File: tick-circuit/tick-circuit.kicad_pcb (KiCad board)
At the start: 2 copper layers, 45.7 x 33 mm, 14 parts, among them J1 Power, J2 50/60Hz, U1 74HCT4060, U2 74HCT73, X1 3.93216 MHz

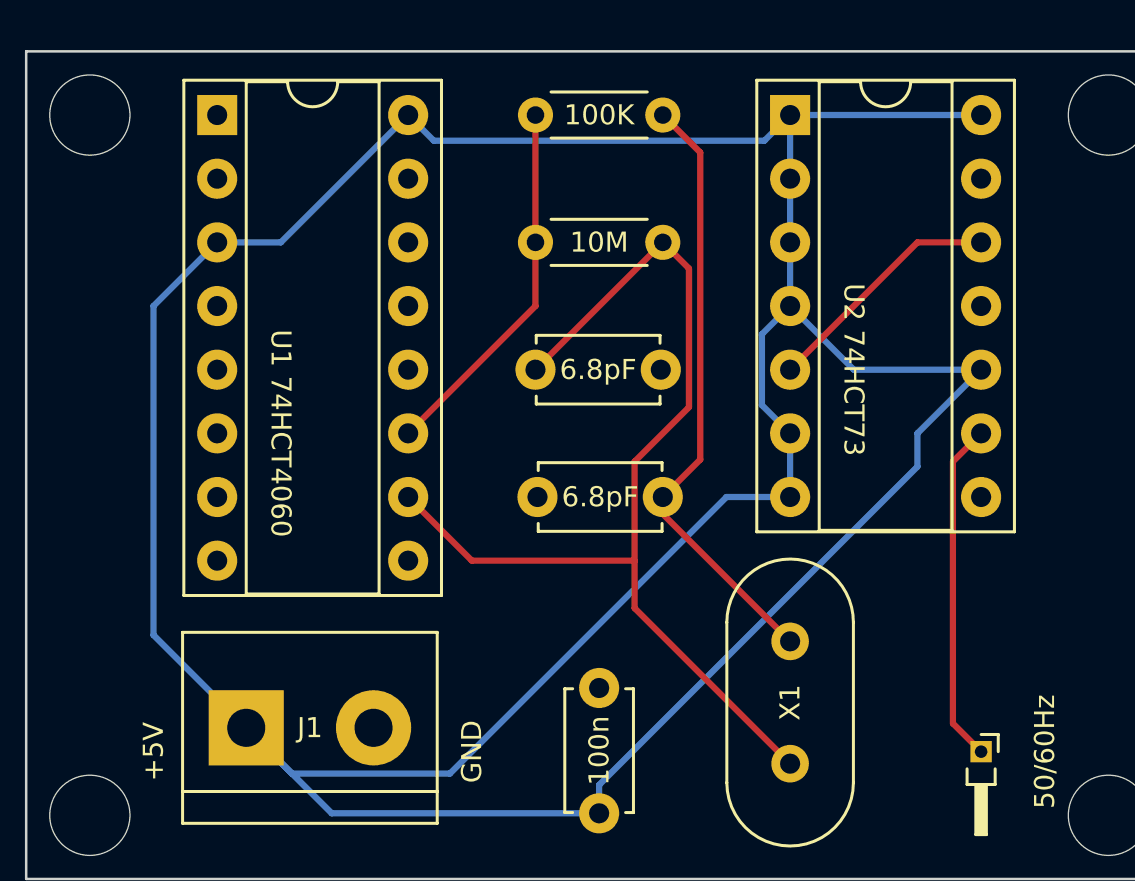
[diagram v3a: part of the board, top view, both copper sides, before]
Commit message: Misconnected +5v to the connection from U1 to U2, which would have sucked
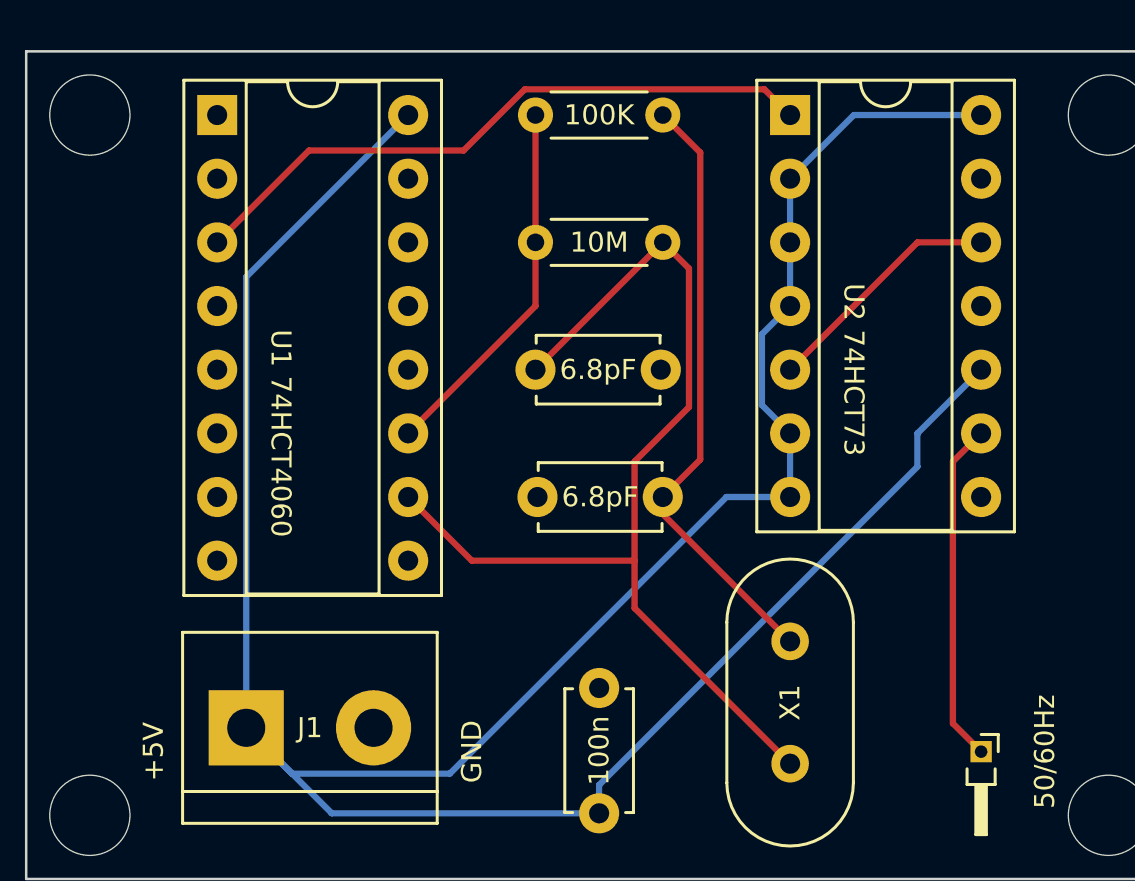
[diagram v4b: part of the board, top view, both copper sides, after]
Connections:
- U1 pad 3: +5V -> Net-(U1-Q13)
- U2 pad 1: +5V -> Net-(U1-Q13)
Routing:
- net +5V: track 146.8 -> 116.0 mm
- net Net-(U1-Q13): track 0.00 -> 25.8 mm
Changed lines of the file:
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@@
   (net 18 "unconnected-(U2A-~{Q}-Pad8)")
   (net 19 "unconnected-(U2B-~{Q}-Pad13)")
+  (net 20 "Net-(U1-Q13)")
   (footprint "Package_DIP:DIP-16_W7.62mm_Socket" (layer "F.Cu")
     (at 33.02 33.02)
@@
       (net 8 "unconnected-(U1-Q12-Pad2)") (pinfunction "Q12") (pintype "output+no_connect"))
     (pad "3" thru_hole oval (at 0 5.08) (size 1.6 1.6) (drill 0.8) (layers "*.Cu" "*.Mask")
-      (net 4 "+5V") (pinfunction "Q13") (pintype "output"))
+      (net 20 "Net-(U1-Q13)") (pinfunction "Q13") (pintype "output"))
     (pad "4" thru_hole oval (at 0 7.62) (size 1.6 1.6) (drill 0.8) (layers "*.Cu" "*.Mask")
       (net 9 "unconnected-(U1-Q5-Pad4)") (pinfunction "Q5") (pintype "output+no_connect"))
@@
       (net 6 "Net-(U1-RS)") (pinfunction "RS") (pintype "input"))
     (pad "12" thru_hole oval (at 7.62 10.16) (size 1.6 1.6) (drill 0.8) (layers "*.Cu" "*.Mask")
-      (net 2 "GND") (pinfunction "MR") (pintype "input"))
+      (net 2 "GND") (pinfunction "MR") (pintype "input") (thermal_bridge_angle 45))
     (pad "13" thru_hole oval (at 7.62 7.62) (size 1.6 1.6) (drill 0.8) (layers "*.Cu" "*.Mask")
       (net 14 "unconnected-(U1-Q8-Pad13)") (pinfunction "Q8") (pintype "output+no_connect"))
@@
       (stroke (width 0.1) (type solid)) (layer "F.Fab"))
     (pad "1" thru_hole rect (at 0 0) (size 1.6 1.6) (drill 0.8) (layers "*.Cu" "*.Mask")
-      (net 4 "+5V") (pinfunction "C") (pintype "input"))
+      (net 20 "Net-(U1-Q13)") (pinfunction "C") (pintype "input"))
     (pad "2" thru_hole oval (at 0 2.54) (size 1.6 1.6) (drill 0.8) (layers "*.Cu" "*.Mask")
       (net 4 "+5V") (pinfunction "~{R}") (pintype "input"))
@@
   (segment (start 60.96 47.04863) (end 60.96 45.72) (width 0.25) (layer "B.Cu") (net 4))
   (segment (start 37.59 60.88) (end 34.18 57.47) (width 0.25) (layer "B.Cu") (net 4))
-  (segment (start 58.42 43.18) (end 55.88 40.64) (width 0.25) (layer "B.Cu") (net 4))
-  (segment (start 63.5 43.18) (end 58.42 43.18) (width 0.25) (layer "B.Cu") (net 4))
-  (segment (start 54.855 34.045) (end 41.665 34.045) (width 0.25) (layer "B.Cu") (net 4))
-  (segment (start 33.02 38.1) (end 30.48 40.64) (width 0.25) (layer "B.Cu") (net 4))
-  (segment (start 30.48 40.64) (end 30.48 53.77) (width 0.25) (layer "B.Cu") (net 4))
+  (segment (start 58.42 33.02) (end 55.88 35.56) (width 0.25) (layer "B.Cu") (net 4))
+  (segment (start 40.64 33.02) (end 34.18 39.48) (width 0.25) (layer "B.Cu") (net 4))
   (segment (start 54.755 41.765) (end 55.88 40.64) (width 0.25) (layer "B.Cu") (net 4))
   (segment (start 48.26 60.88) (end 37.59 60.88) (width 0.25) (layer "B.Cu") (net 4))
-  (segment (start 55.88 33.02) (end 63.5 33.02) (width 0.25) (layer "B.Cu") (net 4))
   (segment (start 48.26 60.88) (end 48.26 59.74863) (width 0.25) (layer "B.Cu") (net 4))
-  (segment (start 55.88 33.02) (end 55.88 35.56) (width 0.25) (layer "B.Cu") (net 4))
-  (segment (start 30.48 53.77) (end 34.18 57.47) (width 0.25) (layer "B.Cu") (net 4))
   (segment (start 60.96 45.72) (end 63.5 43.18) (width 0.25) (layer "B.Cu") (net 4))
   (segment (start 55.88 38.1) (end 55.88 40.64) (width 0.25) (layer "B.Cu") (net 4))
-  (segment (start 33.02 38.1) (end 35.56 38.1) (width 0.25) (layer "B.Cu") (net 4))
-  (segment (start 41.665 34.045) (end 40.64 33.02) (width 0.25) (layer "B.Cu") (net 4))
   (segment (start 53.34 48.26) (end 55.88 48.26) (width 0.25) (layer "B.Cu") (net 4))
   (segment (start 36.005 59.295) (end 42.305 59.295) (width 0.25) (layer "B.Cu") (net 4))
@@
   (segment (start 54.755 44.595) (end 54.755 41.765) (width 0.25) (layer "B.Cu") (net 4))
   (segment (start 55.88 35.56) (end 55.88 38.1) (width 0.25) (layer "B.Cu") (net 4))
-  (segment (start 35.56 38.1) (end 40.64 33.02) (width 0.25) (layer "B.Cu") (net 4))
-  (segment (start 55.88 33.02) (end 54.855 34.045) (width 0.25) (layer "B.Cu") (net 4))
   (segment (start 55.88 45.72) (end 54.755 44.595) (width 0.25) (layer "B.Cu") (net 4))
+  (segment (start 34.18 39.48) (end 34.18 57.47) (width 0.25) (layer "B.Cu") (net 4))
   (segment (start 55.88 48.26) (end 55.88 45.72) (width 0.25) (layer "B.Cu") (net 4))
   (segment (start 34.18 57.47) (end 36.005 59.295) (width 0.25) (layer "B.Cu") (net 4))
   (segment (start 42.305 59.295) (end 53.34 48.26) (width 0.25) (layer "B.Cu") (net 4))
+  (segment (start 63.5 33.02) (end 58.42 33.02) (width 0.25) (layer "B.Cu") (net 4))
   (segment (start 62.375 46.845) (end 63.5 45.72) (width 0.25) (layer "F.Cu") (net 5))
   (segment (start 62.375 57.295) (end 62.375 46.845) (width 0.25) (layer "F.Cu") (net 5))
   (segment (start 63.5 58.42) (end 62.375 57.295) (width 0.25) (layer "F.Cu") (net 5))
-  (segment (start 45.72 40.64) (end 45.72 38.1) (width 0.25) (layer "F.Cu") (net 6))
-  (segment (start 40.64 45.72) (end 45.72 40.64) (width 0.25) (layer "F.Cu") (net 6))
+  (segment (start 45.72 40.64) (end 40.64 45.72) (width 0.25) (layer "F.Cu") (net 6))
   (segment (start 45.72 33.02) (end 45.72 38.1) (width 0.25) (layer "F.Cu") (net 6))
+  (segment (start 45.72 38.1) (end 45.72 40.64) (width 0.25) (layer "F.Cu") (net 6))
   (segment (start 60.96 38.1) (end 55.88 43.18) (width 0.25) (layer "F.Cu") (net 17))
   (segment (start 63.5 38.1) (end 60.96 38.1) (width 0.25) (layer "F.Cu") (net 17))
+  (segment (start 54.855 31.995) (end 55.88 33.02) (width 0.25) (layer "F.Cu") (net 20))
+  (segment (start 45.295431 31.995) (end 54.855 31.995) (width 0.25) (layer "F.Cu") (net 20))
+  (segment (start 36.685 34.435) (end 42.855431 34.435) (width 0.25) (layer "F.Cu") (net 20))
+  (segment (start 33.02 38.1) (end 36.685 34.435) (width 0.25) (layer "F.Cu") (net 20))
+  (segment (start 42.855431 34.435) (end 45.295431 31.995) (width 0.25) (layer "F.Cu") (net 20))
   (zone (net 2) (net_name "GND") (layer "F.Cu") (hatch edge 0.5)
     (connect_pads (clearance 0.5))

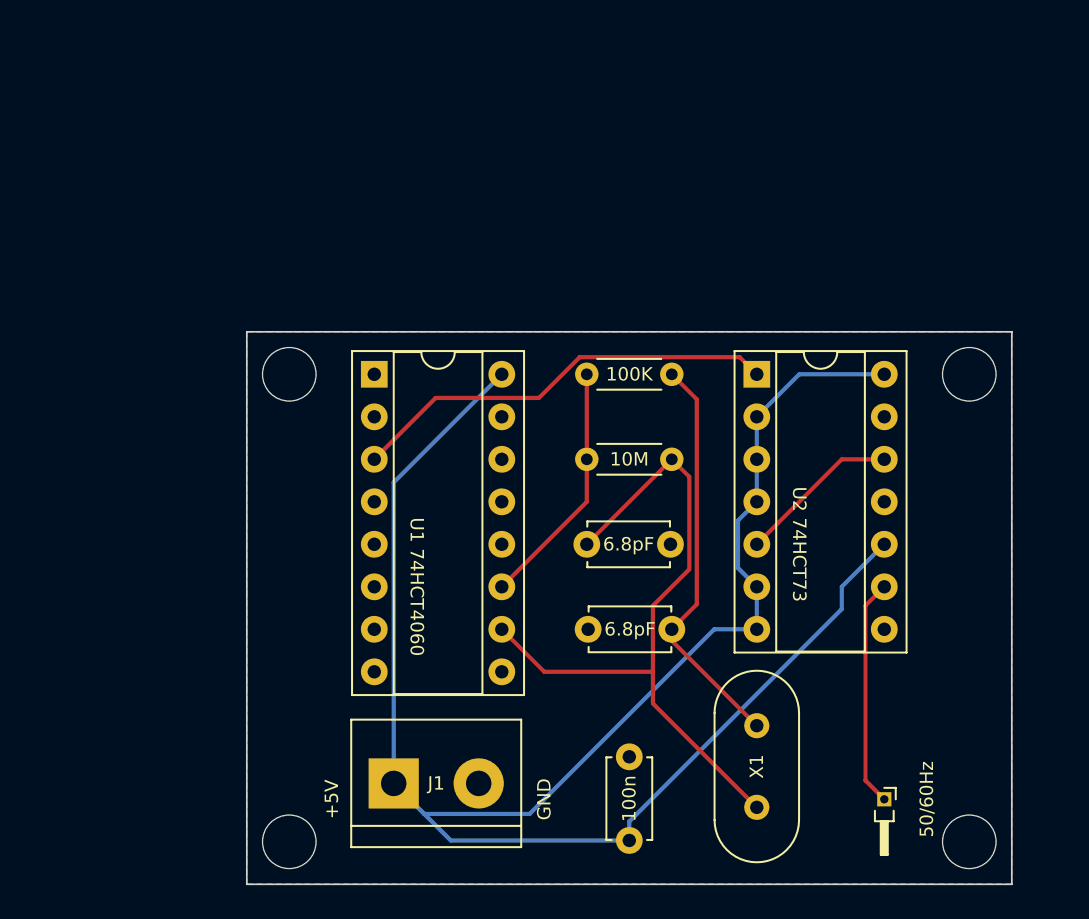
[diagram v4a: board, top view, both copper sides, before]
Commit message: Tick circuit fixes (#4)
* Change resistor footprints, change J2 footprint, alter routing to match, move 5v away from gnd, add URL to pcb

* Add gerber
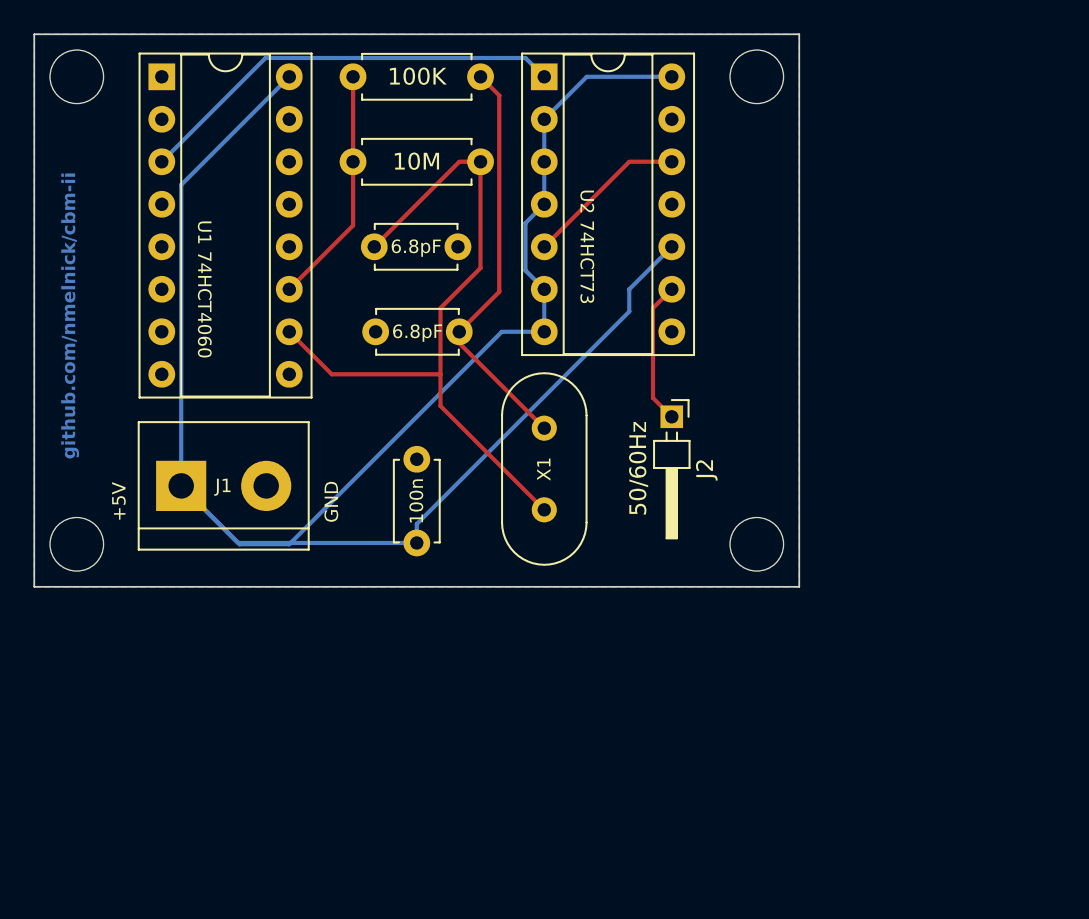
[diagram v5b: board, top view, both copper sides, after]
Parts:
- J2: footprint Connector_PinHeader_1.00mm:PinHeader_1x01_P1.00mm_Horizontal -> Connector_PinHeader_2.00mm:PinHeader_1x01_P2.00mm_Horizontal
- R1, R2: footprint Resistor_THT:R_Axial_DIN0204_L3.6mm_D1.6mm_P5.08mm_Horizontal -> Resistor_THT:R_Axial_DIN0207_L6.3mm_D2.5mm_P7.62mm_Horizontal
- moved J2 26.2 mm to (50.8, 35.6)
- moved R2 22.6 mm to (31.8, 15.2)
- moved U1 21.8 mm to (20.3, 15.2)
- moved U2 21.8 mm to (43.2, 15.2)
- moved X1 21.8 mm to (43.2, 41.1)
- moved J1 21.8 mm to (21.5, 39.7)
- moved REF** 21.8 mm to (15.2, 43.2)
- moved REF** 21.8 mm to (15.2, 15.2)
- moved C1 21.8 mm to (33.0, 25.4)
- moved C2 21.8 mm to (38.1, 30.5)
- moved C3 21.8 mm to (35.6, 43.1)
- moved REF** 21.8 mm to (55.9, 43.2)
- moved REF** 21.8 mm to (55.9, 15.2)
- moved R1 21.1 mm to (39.4, 20.3)
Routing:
- net Net-(J2-Pin_1): track 13.6 -> 8.55 mm
- net +5V: track 116.0 -> 117.3 mm
- net Net-(U1-RTC): track 42.5 -> 43.4 mm
- net Net-(U1-RS): track 14.8 -> 14.1 mm
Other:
- board text added: "github.com/nmelnick/cbm-ii"

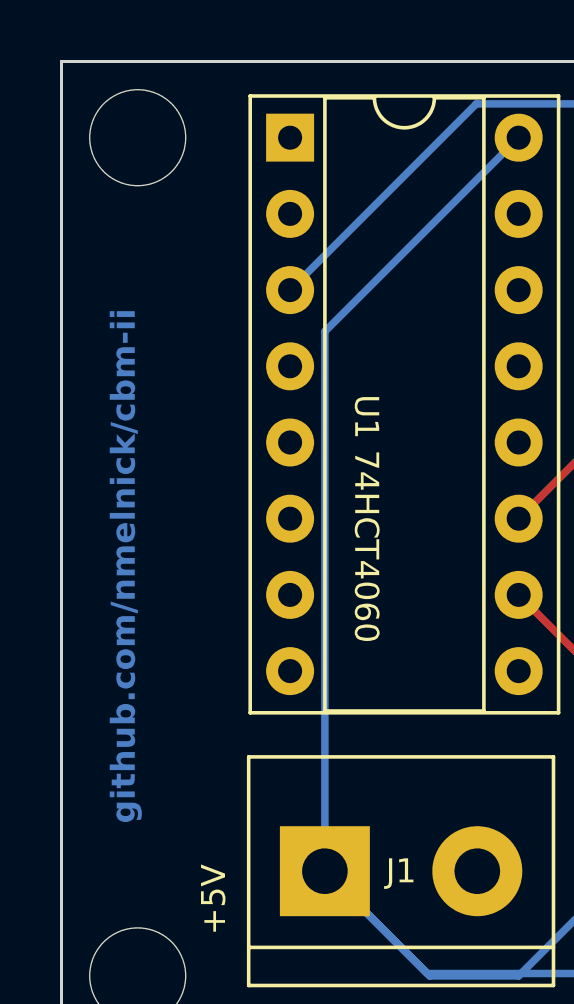
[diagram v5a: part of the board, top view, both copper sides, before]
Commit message: Add name of project
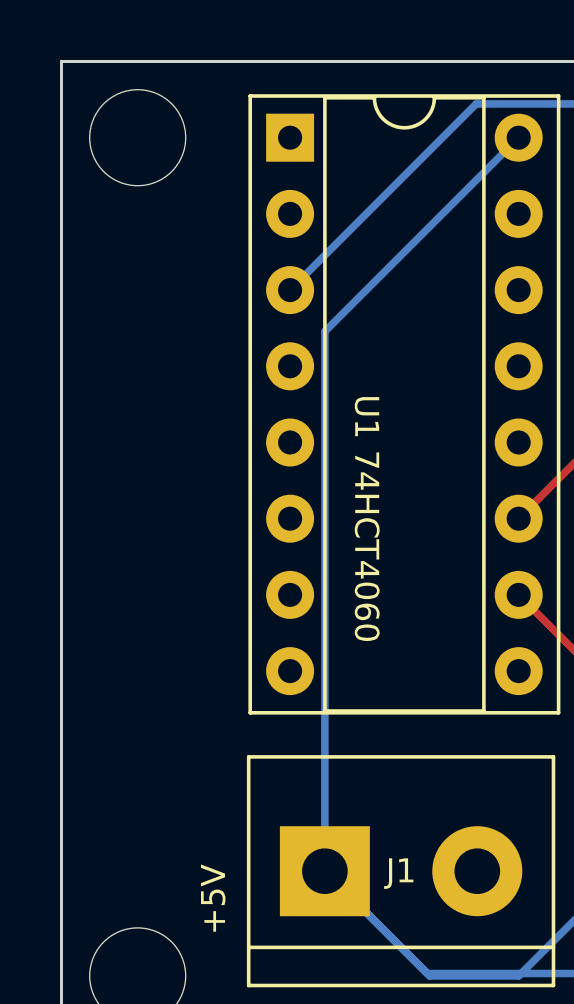
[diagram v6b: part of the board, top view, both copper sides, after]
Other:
- board text added: "tick circuit github.com/nmelnick/cbm-ii"
- board text removed: "github.com/nmelnick/cbm-ii"
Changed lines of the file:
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@@
       (drillshape 0)
       (scaleselection 1)
-      (outputdirectory "/home/nmelnick/src/cbm-ii/tcg/")
+      (outputdirectory "/home/nmelnick/src/cbm-ii/tick-circuit/gerber/")
     )
   )
@@
   (gr_rect (start 12.7 12.7) (end 58.42 45.72)
     (stroke (width 0.1) (type default)) (fill none) (layer "Edge.Cuts"))
-  (gr_text "github.com/nmelnick/cbm-ii" (at 15.24 38.1 90) (layer "B.Cu")
+  (gr_text "tick circuit\ngithub.com/nmelnick/cbm-ii" (at 17 38.1 90) (layer "B.SilkS")
     (effects (font (size 0.8 0.8) (thickness 0.2) bold) (justify left bottom))
   )
